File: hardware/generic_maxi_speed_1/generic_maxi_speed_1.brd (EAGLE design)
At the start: 50 x 50 mm, 31 parts, among them IC1 MEGA168/328, IC2 RFM12, IC3 LP2950Z, Q1 20MHz

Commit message: add holes
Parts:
- D1: value 1N4148DO35-7 -> 1N4148
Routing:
- net N$8: track 104.9 -> 104.0 mm
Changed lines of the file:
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@@
 <layers>
 <layer number="1" name="Top" color="4" fill="1" visible="no" active="yes"/>
-<layer number="16" name="Bottom" color="1" fill="1" visible="no" active="yes"/>
+<layer number="16" name="Bottom" color="1" fill="1" visible="yes" active="yes"/>
 <layer number="17" name="Pads" color="2" fill="1" visible="yes" active="yes"/>
 <layer number="18" name="Vias" color="2" fill="1" visible="yes" active="yes"/>
 <layer number="19" name="Unrouted" color="6" fill="1" visible="no" active="yes"/>
 <layer number="20" name="Dimension" color="15" fill="1" visible="yes" active="yes"/>
-<layer number="21" name="tPlace" color="7" fill="1" visible="yes" active="yes"/>
-<layer number="22" name="bPlace" color="7" fill="1" visible="yes" active="yes"/>
+<layer number="21" name="tPlace" color="7" fill="1" visible="no" active="yes"/>
+<layer number="22" name="bPlace" color="7" fill="1" visible="no" active="yes"/>
 <layer number="23" name="tOrigins" color="15" fill="1" visible="no" active="yes"/>
 <layer number="24" name="bOrigins" color="15" fill="1" visible="no" active="yes"/>
 <layer number="25" name="tNames" color="7" fill="1" visible="yes" active="yes"/>
 <layer number="26" name="bNames" color="7" fill="1" visible="yes" active="yes"/>
-<layer number="27" name="tValues" color="7" fill="1" visible="no" active="yes"/>
-<layer number="28" name="bValues" color="7" fill="1" visible="no" active="yes"/>
+<layer number="27" name="tValues" color="7" fill="1" visible="yes" active="yes"/>
+<layer number="28" name="bValues" color="7" fill="1" visible="yes" active="yes"/>
 <layer number="29" name="tStop" color="7" fill="3" visible="no" active="yes"/>
 <layer number="30" name="bStop" color="7" fill="6" visible="no" active="yes"/>
@@
 <text x="40.005" y="21.2725" size="1.27" layer="25" font="vector" rot="R270">Generic Maxi</text>
 <text x="41.91" y="21.2725" size="1.27" layer="25" font="vector" rot="R270">Speed 1</text>
-<text x="1.5875" y="45.4025" size="1.27" layer="25" font="vector">Rev 1.0</text>
+<text x="24.765" y="48.26" size="1.27" layer="25" font="vector">Rev 1.0</text>
 <rectangle x1="41.6852125" y1="5.487671875" x2="44.8983125" y2="5.515609375" layer="25" rot="R90"/>
 <rectangle x1="41.6153625" y1="5.501640625" x2="44.91228125" y2="5.529578125" layer="25" rot="R90"/>
@@
 <attribute name="MF" value="" x="99.06" y="17.78" size="1.778" layer="27" display="off"/>
 <attribute name="OC_FARNELL" value="176432" x="99.06" y="17.78" size="1.778" layer="27" display="off"/>
-<attribute name="NAME" x="44.577" y="46.228" size="1.27" layer="25" ratio="10"/>
-<attribute name="VALUE" x="44.577" y="44.45" size="1.27" layer="27" ratio="10"/>
+<attribute name="NAME" x="34.163" y="47.752" size="1.27" layer="25" ratio="10" rot="R180"/>
+<attribute name="VALUE" x="34.163" y="46.0375" size="1.27" layer="27" ratio="10" rot="R180"/>
 </element>
 <element name="C5" library="rcl" package="E1,8-4" value="10µ" x="29.21" y="2.54" smashed="yes" rot="R90">
@@
 </element>
 <element name="C4" library="rcl" package="C025-030X050" value="220n" x="29.845" y="22.225" smashed="yes" rot="R180">
-<attribute name="NAME" x="32.9565" y="21.9075" size="1.27" layer="25" ratio="10"/>
-<attribute name="VALUE" x="33.274" y="20.1295" size="1.27" layer="27" ratio="10"/>
+<attribute name="NAME" x="32.9565" y="20.6375" size="1.27" layer="25" ratio="10"/>
+<attribute name="VALUE" x="32.9565" y="22.352" size="1.27" layer="27" ratio="10"/>
 </element>
 <element name="JP2" library="pinhead" package="1X01" value="ANT" x="47.625" y="1.905" smashed="yes">
@@
 <attribute name="VALUE" x="8.8265" y="9.525" size="1.27" layer="27" ratio="10" rot="R180"/>
 </element>
-<element name="D1" library="diode" package="DO35-7" value="1N4148DO35-7" x="10.795" y="2.54" smashed="yes" rot="R180">
-<attribute name="NAME" x="5.1435" y="3.175" size="1.27" layer="25" ratio="10" rot="R180"/>
+<element name="D1" library="diode" package="DO35-7" value="1N4148" x="10.795" y="2.54" smashed="yes" rot="R180">
+<attribute name="NAME" x="8.3185" y="4.7625" size="1.27" layer="25" ratio="10" rot="R180"/>
+<attribute name="VALUE" x="12.954" y="3.3655" size="1.27" layer="27" ratio="10"/>
 </element>
 <element name="R5" library="rcl" package="0207/7" value="1k" x="26.035" y="13.6525" smashed="yes" rot="R270">
@@
 <wire x1="41.91" y1="33.02" x2="41.91" y2="41.275" width="0.4064" layer="16"/>
 <wire x1="41.91" y1="41.275" x2="45.4025" y2="41.275" width="0.4064" layer="16"/>
-<wire x1="45.4025" y1="41.275" x2="45.4025" y2="46.0375" width="0.4064" layer="16"/>
+<wire x1="45.4025" y1="41.275" x2="45.4025" y2="44.45" width="0.4064" layer="16"/>
 <wire x1="6.35" y1="48.26" x2="35.8394" y2="48.26" width="0.4064" layer="16"/>
 <wire x1="35.8394" y1="48.26" x2="36.1188" y2="47.9806" width="0.4064" layer="16" curve="-90"/>
-<wire x1="36.1188" y1="47.9806" x2="41.91" y2="46.0375" width="0.4064" layer="16"/>
-<wire x1="41.91" y1="46.0375" x2="45.4025" y2="46.0375" width="0.4064" layer="16"/>
+<wire x1="36.1188" y1="47.9806" x2="42.2275" y2="45.72" width="0.4064" layer="16"/>
+<wire x1="42.2275" y1="45.72" x2="44.45" y2="45.72" width="0.4064" layer="16"/>
+<wire x1="44.45" y1="45.72" x2="45.4025" y2="44.45" width="0.4064" layer="16"/>
 </signal>
 <signal name="N$12">
@@
 <wire x1="34.29" y1="4.32" x2="34.26" y2="4.32" width="0.4064" layer="16"/>
 </signal>
+<signal name="N$13">
+<via x="2.8575" y="47.3075" extent="1-16" drill="2"/>
+<via x="2.8575" y="3.175" extent="1-16" drill="2"/>
+<via x="46.99" y="47.3075" extent="1-16" drill="2"/>
+</signal>
 </signals>

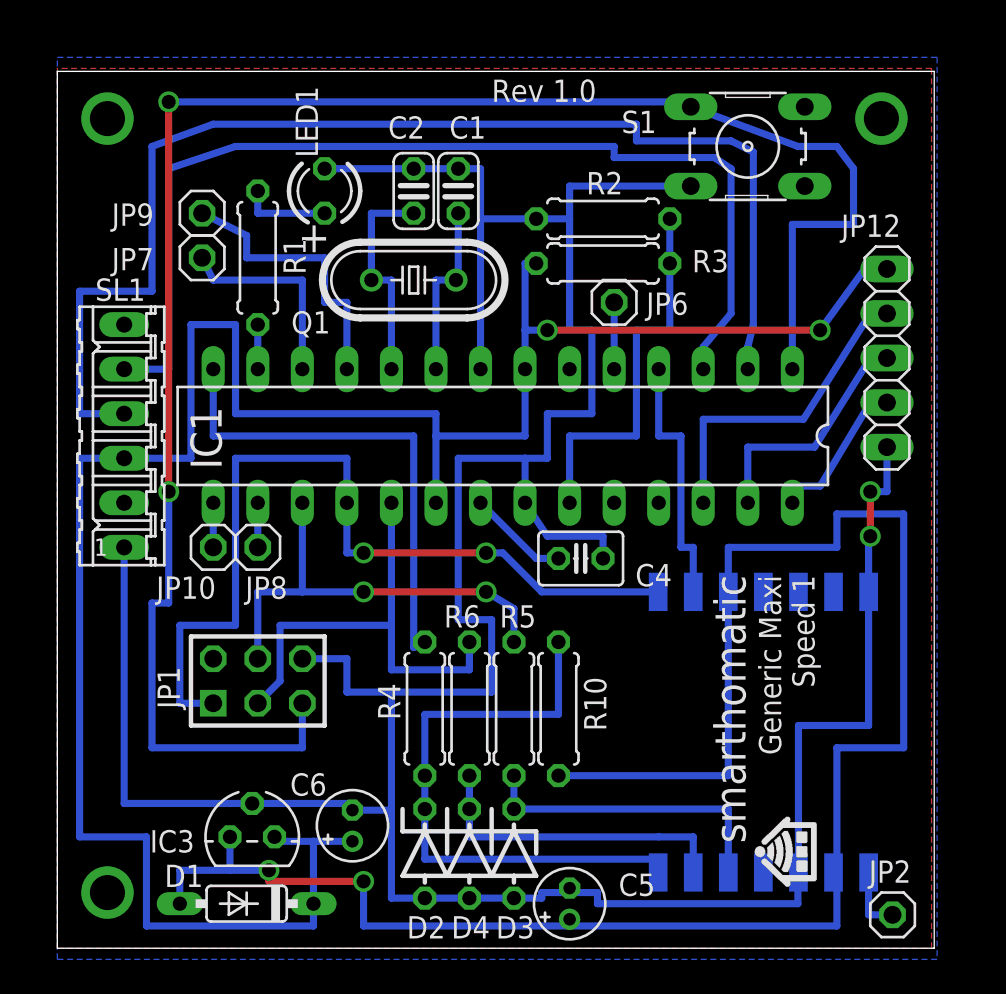
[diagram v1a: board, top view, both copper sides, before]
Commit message: Generic Maxi Speed V1.1 includes a solder switch to turn on the VCC pin of the ISP connector.
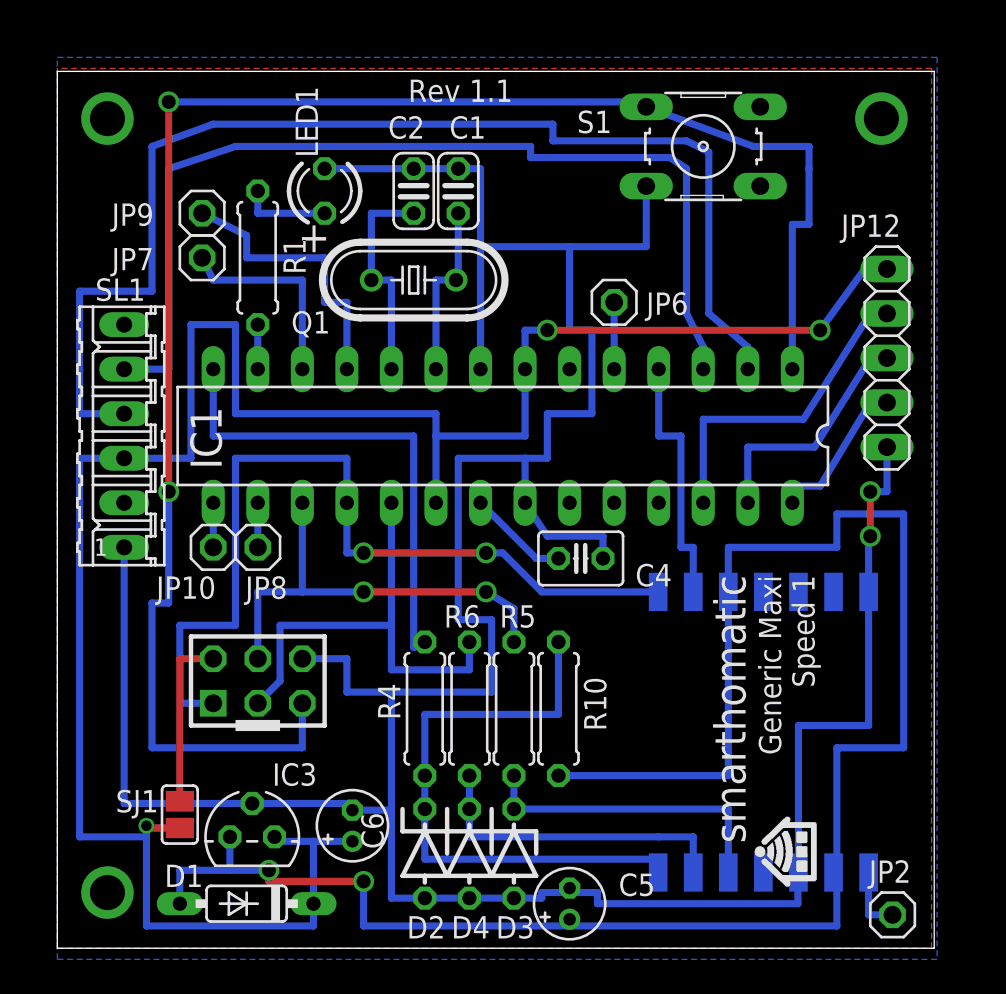
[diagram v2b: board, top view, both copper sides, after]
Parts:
- removed R2: 150k, rcl:0207/7
- removed R3: 330k, rcl:0207/7
- added SJ1: VCC, jumper:SJ
- moved S1 2.54 mm to (36.8, 45.7)
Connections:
- net +5V: now also SJ1.2; no longer R3.2
- net GND: no longer R2.1
- net N$18: now also JP1.2, SJ1.1; no longer IC1.23, R2.2, R3.1
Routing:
- net N$18: track 21.9 -> 10.0 mm
- net GND: track 191.1 -> 195.8 mm
- net N$8: track 104.0 -> 99.6 mm
- net N$9: track 59.1 -> 56.2 mm
- net +5V: track 125.6 -> 123.8 mm, vias 2 -> 3
- net N$10: track 69.9 -> 68.4 mm
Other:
- board text added: "Rev 1.1"
- board text removed: "Rev 1.0"

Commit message: Generic Maxi Speed V1.2: Added transistor to switch power of RFM module to allow restart or module if transceiver doesn't react anymore.
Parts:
- added C3: 1µ, rcl:C025-030X050
- added Q2: BC327, transistor-pnp:TO92
- added R2: 560R, rcl:0207/7
- moved C4 2.43 mm to (27.5, 21.7)
- moved JP1 1.27 mm to (10.2, 15.2)
- moved R10 1.27 mm to (27.3, 13.7)
- moved R4 1.27 mm to (19.7, 13.7)
- moved R5 1.27 mm to (24.8, 13.7)
- moved R6 1.27 mm to (22.2, 13.7)
- moved IC2 0.64 mm to (48.3, 19.7)
- moved JP2 0.45 mm to (47.9, 1.59)
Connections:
- new net N$28: IC1.26, R2.2
- new net N$29: Q2.2, R2.1
- new net N$32: C3.2, IC2.3, IC2.9, Q2.3
- net +3V3: now also Q2.1; no longer IC2.3, IC2.9
- net GND: now also C3.1
- net N$14: now also IC1.25; no longer IC1.26
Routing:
- net N$32: track 0.00 -> 54.8 mm, vias 0 -> 1
- net +3V3: track 107.5 -> 59.4 mm
- net N$28: track 0.00 -> 14.9 mm, vias 0 -> 2
- net N$14: track 18.6 -> 33.4 mm
- net GND: track 195.8 -> 201.3 mm, vias 2 -> 0
- net N$29: track 0.00 -> 4.96 mm
- net N$24: track 5.76 -> 4.26 mm
- net N$18: track 10.0 -> 11.3 mm
- net N$8: track 99.6 -> 100.9 mm
- net N$5: track 18.3 -> 19.3 mm
- net N$16: track 17.7 -> 18.8 mm
- net N$26: track 28.0 -> 27.2 mm
- net N$27: track 34.1 -> 33.3 mm
- net N$15: track 14.7 -> 15.3 mm
- net N$3: track 25.7 -> 25.0 mm
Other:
- board text added: "Rev 1.2"
- board text removed: "Rev 1.1"
